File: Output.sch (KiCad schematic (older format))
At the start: 12 parts, among them J4 Micro_SD_Card, J5 ST_01x02, Q1 DMN2230U

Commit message: Pyro
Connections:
- net at Q1.3 (D): now also J5.2 (Pin_2)
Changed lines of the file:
@@
 Text HLabel 4700 4050 0    39   Input ~ 0
 PYRO_1
+Wire Wire Line
+	5225 3900 5225 3725
+Wire Wire Line
+	5225 3725 5600 3725
 $EndSCHEMATC

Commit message: rc and cont on pyro, linear reg, flash
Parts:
- added C?: 470uF, symbol Device:C_Small
- added R?: 100K, symbol Device:R_Small
- added R?: 20K, symbol Device:R_Small
- added R?: 10K, symbol Device:R_Small
- added R?: 200R, symbol Device:R_Small
- added R?: 150R, symbol Device:R_Small
- added R?: 5R, symbol Device:R_Small
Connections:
- net +12V: now also R?.2; no longer J5.1 (Pin_1)
- net GND: now also C?.1, R?.2, R?.2, R?.2
- net PYRO_1: now also R?.2
- net at Q1.1 (G): now also R?.1, R?.1
- net at Q1.2 (S): now also R?.1
- net at J5.2 (Pin_2), Q1.3 (D): now also R?.1
- new net: C?.2, J5.1 (Pin_1), R?.1
- new net PYRO_CONT: R?.1, R?.2
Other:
- moved on the sheet: C12, C?, J4, J5, Q1, U?

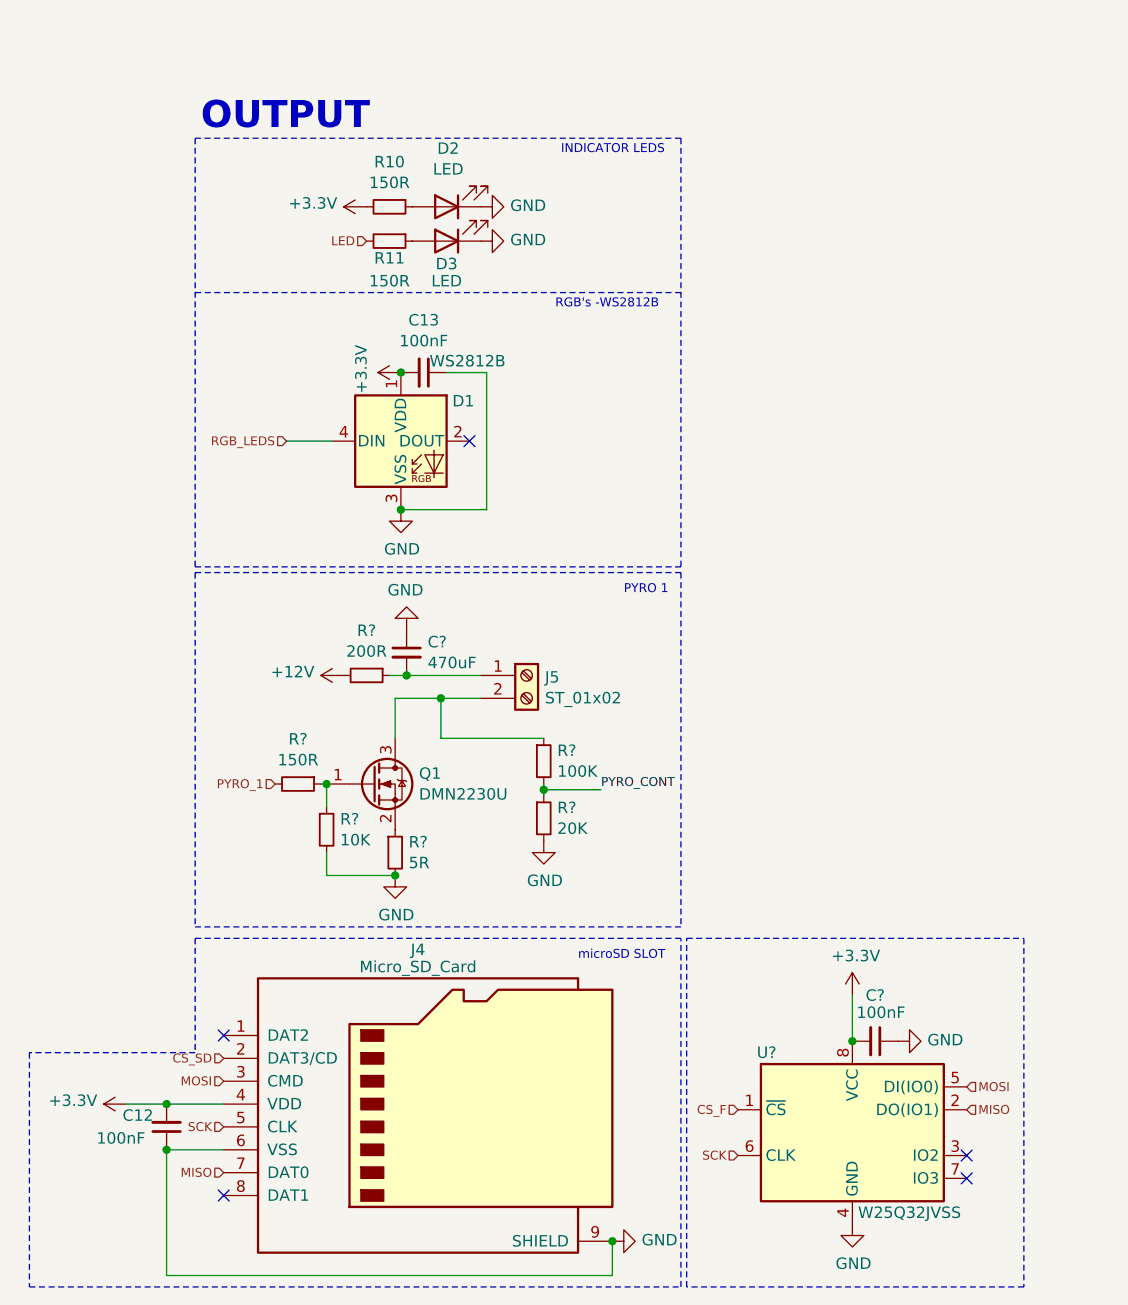
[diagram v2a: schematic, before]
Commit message: bno055 removed, bmi088, schotksy
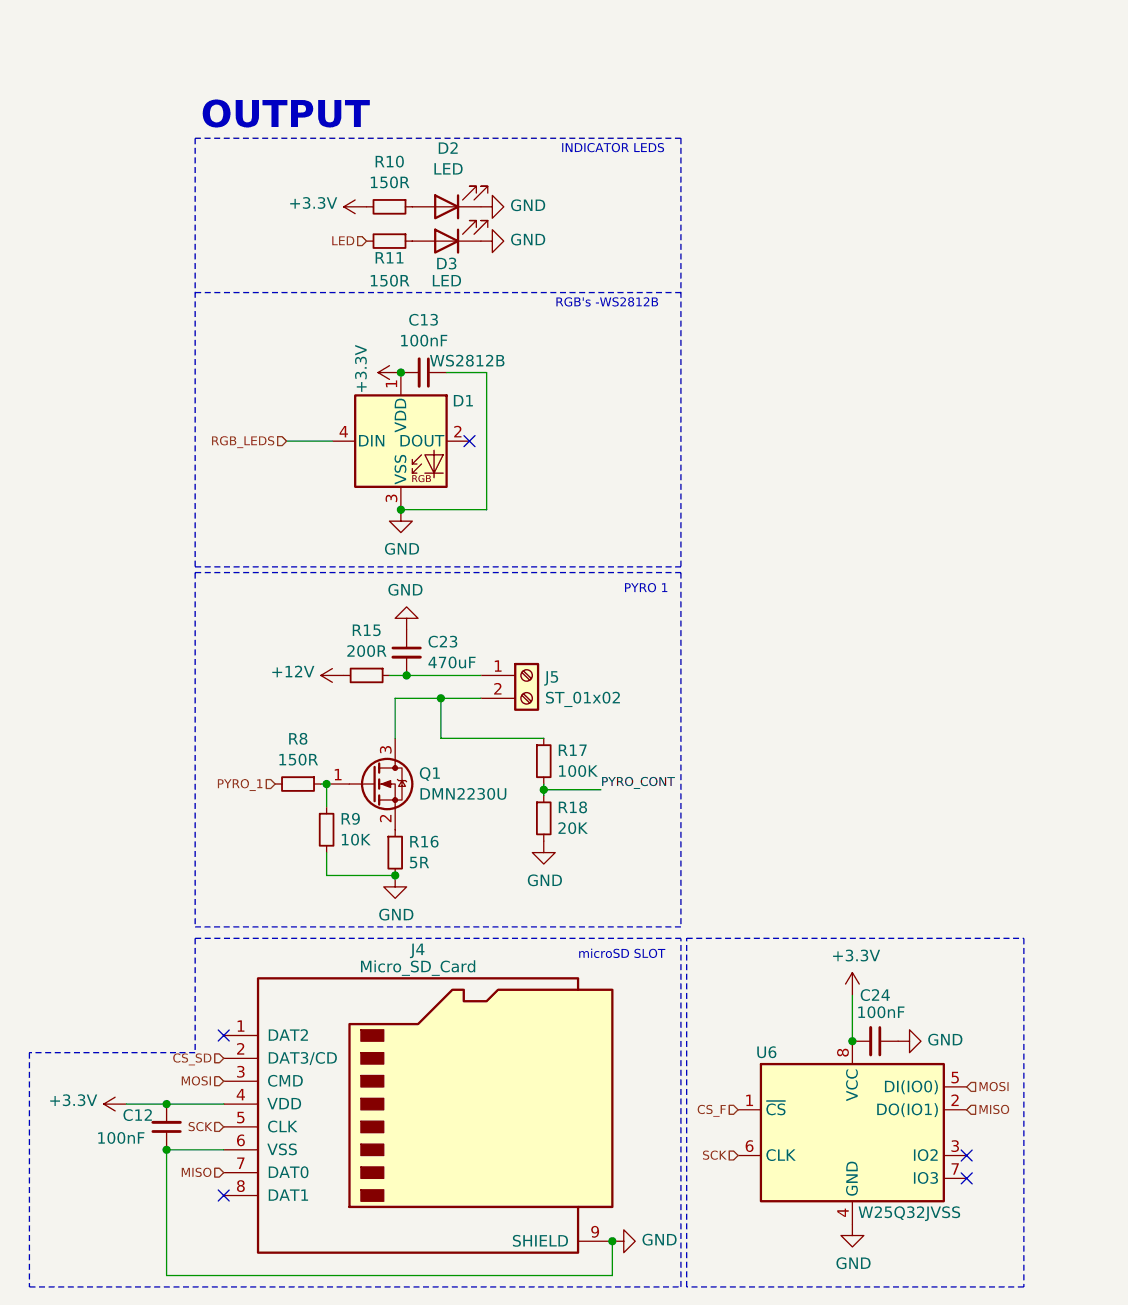
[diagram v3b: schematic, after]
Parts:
- C23, C24: renamed from C?; footprint (none) -> Capacitor_SMD:C_0603_1608Metric
- R15, R16, R17, R18, R8, R9: renamed from R?; footprint (none) -> Capacitor_SMD:C_0603_1608Metric
- gave numbers to parts that had none: 1
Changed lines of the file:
@@
 	5475 2675 5650 2675
 $Comp
-L Memory_Flash:W25Q32JVSS U?
+L Memory_Flash:W25Q32JVSS U6
 U 1 1 604A0554
 P 7250 6000
-F 0 "U?" H 6875 6350 50  0000 C CNN
+F 0 "U6" H 6875 6350 50  0000 C CNN
 F 1 "W25Q32JVSS" H 7500 5650 50  0000 C CNN
 F 2 "Package_SO:SOIC-8_5.23x5.23mm_P1.27mm" H 7250 6000 50  0001 C CNN
@@
 $EndComp
 $Comp
-L Device:C_Small C?
+L Device:C_Small C24
 U 1 1 604A5375
 P 7350 5600
-F 0 "C?" V 7150 5600 50  0000 C CNN
+F 0 "C24" V 7150 5600 50  0000 C CNN
 F 1 "100nF" V 7225 5625 50  0000 C CNN
-F 2 "" H 7350 5600 50  0001 C CNN
+F 2 "Capacitor_SMD:C_0603_1608Metric" H 7350 5600 50  0001 C CNN
 F 3 "~" H 7350 5600 50  0001 C CNN
 	1    7350 5600
@@
 $EndComp
 $Comp
-L power:+3.3V #PWR?
+L power:+3.3V #PWR0144
 U 1 1 604A58ED
 P 7250 5400
-F 0 "#PWR?" H 7250 5250 50  0001 C CNN
+F 0 "#PWR0144" H 7250 5250 50  0001 C CNN
 F 1 "+3.3V" H 7265 5573 50  0000 C CNN
 F 2 "" H 7250 5400 50  0001 C CNN
@@
 Connection ~ 7250 5600
 $Comp
-L power:GND #PWR?
+L power:GND #PWR0145
 U 1 1 604A636A
 P 7450 5600
-F 0 "#PWR?" H 7450 5350 50  0001 C CNN
+F 0 "#PWR0145" H 7450 5350 50  0001 C CNN
 F 1 "GND" V 7455 5472 50  0000 R CNN
 F 2 "" H 7450 5600 50  0001 C CNN
@@
 $EndComp
 $Comp
-L power:GND #PWR?
+L power:GND #PWR0146
 U 1 1 604A6CD7
 P 7250 6400
-F 0 "#PWR?" H 7250 6150 50  0001 C CNN
+F 0 "#PWR0146" H 7250 6150 50  0001 C CNN
 F 1 "GND" H 7255 6227 50  0000 C CNN
 F 2 "" H 7250 6400 50  0001 C CNN
@@
 	5250 4275 5250 4100
 $Comp
-L Device:C_Small C?
+L Device:C_Small C23
 U 1 1 6057B146
 P 5300 3900
-F 0 "C?" H 5392 3946 50  0000 L CNN
+F 0 "C23" H 5392 3946 50  0000 L CNN
 F 1 "470uF" H 5392 3855 50  0000 L CNN
-F 2 "" H 5300 3900 50  0001 C CNN
+F 2 "Capacitor_SMD:C_0603_1608Metric" H 5300 3900 50  0001 C CNN
 F 3 "~" H 5300 3900 50  0001 C CNN
 	1    5300 3900
@@
 	5300 4000 5625 4000
 $Comp
-L power:GND #PWR?
+L power:GND #PWR0147
 U 1 1 6057D63F
 P 5300 3800
-F 0 "#PWR?" H 5300 3550 50  0001 C CNN
+F 0 "#PWR0147" H 5300 3550 50  0001 C CNN
 F 1 "GND" H 5305 3627 50  0000 C CNN
 F 2 "" H 5300 3800 50  0001 C CNN
@@
 Connection ~ 5300 4000
 $Comp
-L Device:R_Small R?
+L Device:R_Small R17
 U 1 1 6057EBF4
 P 5900 4375
-F 0 "R?" H 5959 4421 50  0000 L CNN
+F 0 "R17" H 5959 4421 50  0000 L CNN
 F 1 "100K" H 5959 4330 50  0000 L CNN
-F 2 "" H 5900 4375 50  0001 C CNN
+F 2 "Capacitor_SMD:C_0603_1608Metric" H 5900 4375 50  0001 C CNN
 F 3 "~" H 5900 4375 50  0001 C CNN
 	1    5900 4375
@@
 $EndComp
 $Comp
-L Device:R_Small R?
+L Device:R_Small R18
 U 1 1 6057F23C
 P 5900 4625
-F 0 "R?" H 5959 4671 50  0000 L CNN
+F 0 "R18" H 5959 4671 50  0000 L CNN
 F 1 "20K" H 5959 4580 50  0000 L CNN
-F 2 "" H 5900 4625 50  0001 C CNN
+F 2 "Capacitor_SMD:C_0603_1608Metric" H 5900 4625 50  0001 C CNN
 F 3 "~" H 5900 4625 50  0001 C CNN
 	1    5900 4625
@@
 	5450 4100 5625 4100
 $Comp
-L power:GND #PWR?
+L power:GND #PWR0148
 U 1 1 6058204F
 P 5900 4725
-F 0 "#PWR?" H 5900 4475 50  0001 C CNN
+F 0 "#PWR0148" H 5900 4475 50  0001 C CNN
 F 1 "GND" H 5905 4552 50  0000 C CNN
 F 2 "" H 5900 4725 50  0001 C CNN
@@
 PYRO_CONT
 $Comp
-L Device:R_Small R?
+L Device:R_Small R9
 U 1 1 60585D72
 P 4950 4675
-F 0 "R?" H 5009 4721 50  0000 L CNN
+F 0 "R9" H 5009 4721 50  0000 L CNN
 F 1 "10K" H 5009 4630 50  0000 L CNN
-F 2 "" H 4950 4675 50  0001 C CNN
+F 2 "Capacitor_SMD:C_0603_1608Metric" H 4950 4675 50  0001 C CNN
 F 3 "~" H 4950 4675 50  0001 C CNN
 	1    4950 4675
@@
 $EndComp
 $Comp
-L Device:R_Small R?
+L Device:R_Small R15
 U 1 1 60587D45
 P 5125 4000
-F 0 "R?" V 4929 4000 50  0000 C CNN
+F 0 "R15" V 4929 4000 50  0000 C CNN
 F 1 "200R" V 5020 4000 50  0000 C CNN
-F 2 "" H 5125 4000 50  0001 C CNN
+F 2 "Capacitor_SMD:C_0603_1608Metric" H 5125 4000 50  0001 C CNN
 F 3 "~" H 5125 4000 50  0001 C CNN
 	1    5125 4000
@@
 $EndComp
 $Comp
-L Device:R_Small R?
+L Device:R_Small R8
 U 1 1 60589219
 P 4825 4475
-F 0 "R?" V 4629 4475 50  0000 C CNN
+F 0 "R8" V 4629 4475 50  0000 C CNN
 F 1 "150R" V 4720 4475 50  0000 C CNN
-F 2 "" H 4825 4475 50  0001 C CNN
+F 2 "Capacitor_SMD:C_0603_1608Metric" H 4825 4475 50  0001 C CNN
 F 3 "~" H 4825 4475 50  0001 C CNN
 	1    4825 4475
@@
 	4950 4875 5250 4875
 $Comp
-L power:GND #PWR?
+L power:GND #PWR0149
 U 1 1 605BA4F0
 P 5250 4875
-F 0 "#PWR?" H 5250 4625 50  0001 C CNN
+F 0 "#PWR0149" H 5250 4625 50  0001 C CNN
 F 1 "GND" H 5255 4702 50  0000 C CNN
 F 2 "" H 5250 4875 50  0001 C CNN
@@
 $EndComp
 $Comp
-L Device:R_Small R?
+L Device:R_Small R16
 U 1 1 605BB5AF
 P 5250 4775
-F 0 "R?" H 5309 4821 50  0000 L CNN
+F 0 "R16" H 5309 4821 50  0000 L CNN
 F 1 "5R" H 5309 4730 50  0000 L CNN
-F 2 "" H 5250 4775 50  0001 C CNN
+F 2 "Capacitor_SMD:C_0603_1608Metric" H 5250 4775 50  0001 C CNN
 F 3 "~" H 5250 4775 50  0001 C CNN
 	1    5250 4775

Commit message: Schematic cleanup, pyro
thanks ben for the advice
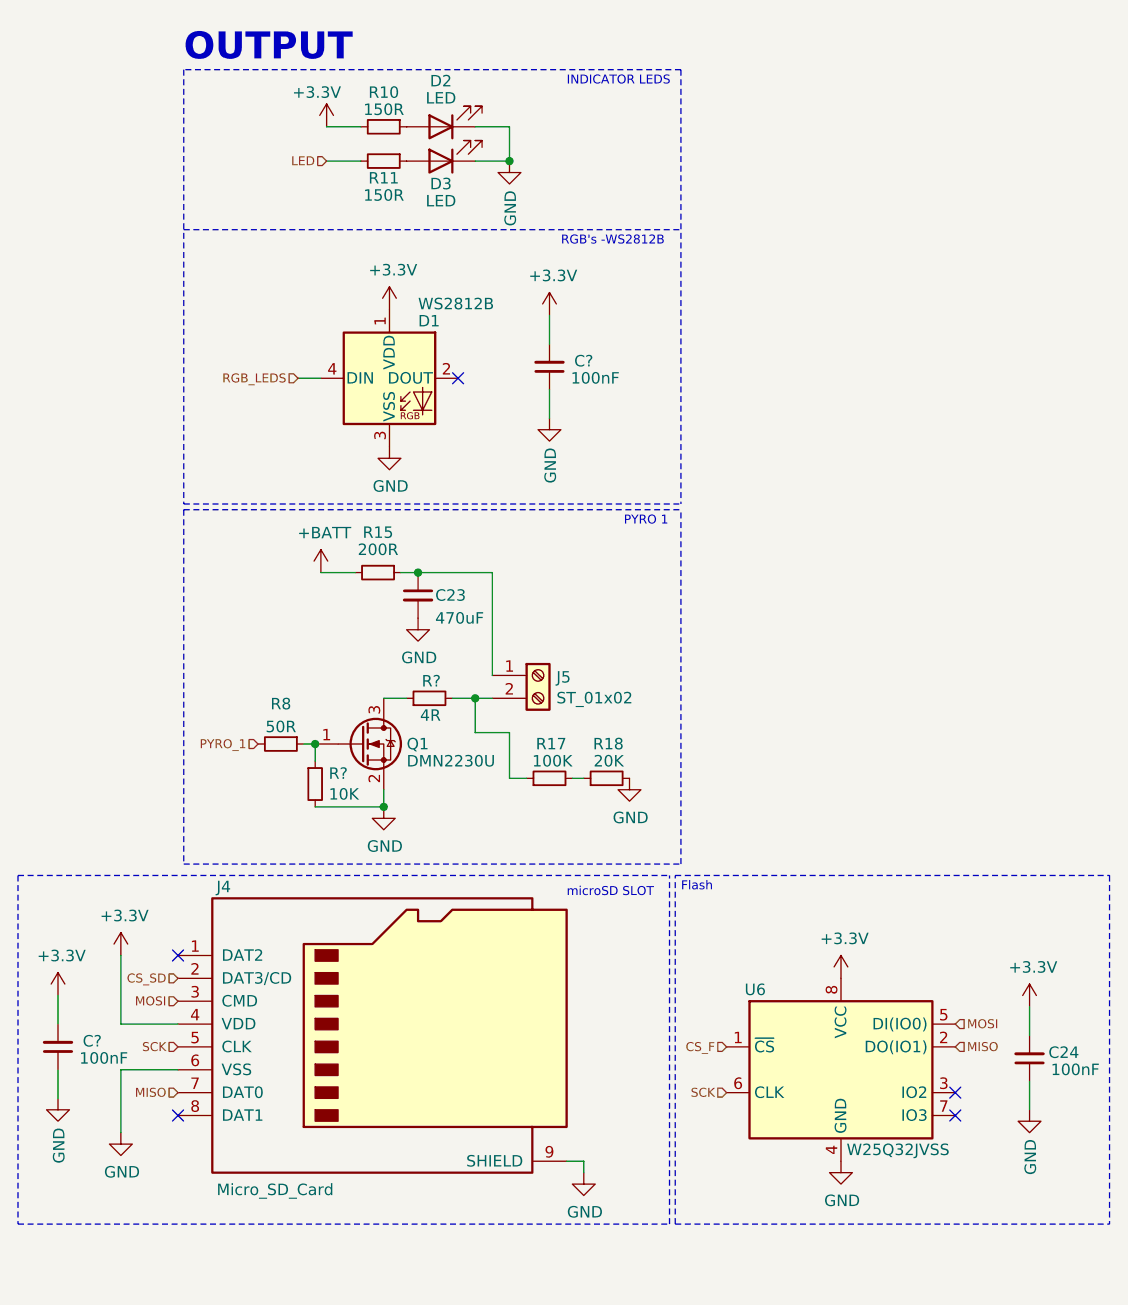
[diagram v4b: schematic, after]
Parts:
- removed C12, C13: 100nF, Capacitor_SMD:C_0603_1608Metric, symbol Device:C_Small
- removed R16: 5R, Capacitor_SMD:C_0603_1608Metric, symbol Device:R_Small
- removed R9: 10K, Capacitor_SMD:C_0603_1608Metric, symbol Device:R_Small
- added C? (x2): 100nF, Capacitor_SMD:C_0603_1608Metric, symbol Device:C_Small
- added R?: 4R, Capacitor_SMD:C_0603_1608Metric, symbol Device:R_Small
- added R?: 10K, Capacitor_SMD:C_0603_1608Metric, symbol Device:R_Small
- R8: value 150R -> 50R
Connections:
- net +3V3: now also C?.2, C?.2
- net GND: now also C23.2, Q1.2 (S), C?.1, C?.1, R?.2; no longer C23.1
- net at Q1.1 (G), R8.1: now also R?.1
- net at J5.2 (Pin_2), R17.1: now also R?.2; no longer Q1.3 (D)
- net at J5.1 (Pin_1), R15.1: now also C23.1; no longer C23.2
- net +12V renamed +BATT
- net PYRO_CONT: no longer names the net of R17.2, R18.1
- new net: Q1.3 (D), R?.1
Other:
- note added: "Flash"
- moved on the sheet: C23, C24, D1, D2, D3, J4, J5, Q1, R10, R11, R15, R17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

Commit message: more cleanup
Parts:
- C23: footprint Capacitor_SMD:C_0603_1608Metric -> Capacitor_SMD:CP_Elec_10x10
- J5: footprint TerminalBlock_Phoenix:TerminalBlock_Phoenix_PT-1,5-2-3.5-H_1x02_P3.50mm_Horizontal -> TerminalBlock:TerminalBlock_bornier-2_P5.08mm
- R10, R11, R15, R17, R18, R8: footprint Capacitor_SMD:C_0603_1608Metric -> Resistor_SMD:R_0603_1608Metric
- R12, R9: renamed from R?; footprint Capacitor_SMD:C_0603_1608Metric -> Resistor_SMD:R_0603_1608Metric
- gave numbers to parts that had none: 2
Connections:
- net PY1_CON: now reaches R17.2, R18.1
- net RGB_LEDS renamed WS2812
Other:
- moved on the sheet: D2, D3, R10, R11
